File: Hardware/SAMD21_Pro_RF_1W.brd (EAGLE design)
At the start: 53.3 x 40.6 mm, 143 parts, among them J10 AVR_SPI_PROG_3X2TESTPOINTS, J12 JST, J13 U.FL, J14 RFM_DIO, J7 PTH, J9 External On/Off, U1 MCP73831, U2 ADJ3.3, U4 ATSAMD21G, U5 4MB Flash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

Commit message: Intermediate save
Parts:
- moved C12 39.5 mm to (22.9, 7.37), turned to 270 degrees
- moved C14 37.9 mm to (24.1, 7.37), turned to 90 degrees
- moved R8 28.3 mm to (29.2, 34.3), turned to 0 degrees
- moved J10 19.0 mm to (27.7, 25.4), turned to 180 degrees
- moved C8 15.1 mm to (23.6, 33.0), turned to 270 degrees
- moved C5 14.4 mm to (22.4, 33.0), turned to 90 degrees
- moved R3 10.7 mm to (24.9, 33.0), turned to 90 degrees
- moved C11 9.55 mm to (15.2, 36.8), turned to 270 degrees
- moved FD2 8.89 mm to (52.1, 36.8)
- moved FD4 8.89 mm to (52.1, 36.8)
- moved JP6 5.08 mm to (45.7, 14.0)
- moved JP1 5.08 mm to (45.7, 16.5)
- moved JP3 3.94 mm to (45.7, 31.1), turned to 180 degrees
- moved U5 2.59 mm to (29.2, 30.5)
- moved JP2 2.54 mm to (45.7, 19.1)
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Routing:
- net 5V: track 0.00 -> 86.8 mm, vias 0 -> 7
- net 3.3V: track 33.1 -> 103.1 mm, vias 4 -> 9
- net USB_VCC: track 0.96 -> 66.1 mm, vias 0 -> 5
- net GND: track 11.4 -> 73.6 mm, vias 5 -> 3
- net SCK: track 2.34 -> 64.6 mm, vias 1 -> 5
- net DIO3: track 0.00 -> 59.8 mm, vias 0 -> 5
- net DIO5: track 0.00 -> 57.0 mm, vias 0 -> 5
- net DIO4: track 0.00 -> 55.5 mm, vias 0 -> 5
- net DIO2: track 0.00 -> 54.1 mm, vias 0 -> 4
- net DIO1: track 0.00 -> 53.8 mm, vias 0 -> 3
- net !RST: track 12.6 -> 65.3 mm, vias 2 -> 3
- net DIO0: track 0.00 -> 52.6 mm, vias 0 -> 3
- net SDA: track 9.58 -> 60.1 mm, vias 1 -> 2
- net SCL: track 10.8 -> 59.0 mm, vias 1 -> 6
- net MISO: track 9.96 -> 57.6 mm, vias 1 -> 6
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- added copper zone on layer 1, net GND
- added copper zone on layer 16, net GND
- removed copper zone on layer 1, net GND1
- removed copper zone on layer 16, net GND1

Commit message: Intermediate
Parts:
- moved J7 0.64 mm to (1.91, 24.1)
- turned C6 to 90 degrees
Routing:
- net 3.3V: track 103.1 -> 212.6 mm, vias 9 -> 20
- net GND: track 73.6 -> 98.0 mm, vias 3 -> 36
- net RAW: track 41.3 -> 62.2 mm, vias 3 -> 6
- net 5V: track 86.8 -> 104.2 mm, vias 7 -> 8
- net MOSI: track 40.2 -> 57.6 mm, vias 4 -> 6
- net !RST: track 65.3 -> 72.6 mm, vias 3 -> 4
- net SHLD: track 0.00 -> 6.97 mm
- net USB_VCC: track 66.1 -> 71.8 mm
- net SWDCLK: track 25.4 -> 30.8 mm
- net MISO: track 57.6 -> 62.3 mm
- net D8_!FLASH_CS: track 20.4 -> 22.7 mm
- net SCK: track 64.6 -> 66.4 mm
- net D-: track 50.1 -> 51.8 mm
- net RXI: track 32.6 -> 34.3 mm
- net MISO5V: track 12.1 -> 13.5 mm
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- added copper zone on layer 1, net SHLD
- added copper zone on layer 16, net SHLD
- removed copper zone on layer 1, net SHLD1
- removed copper zone on layer 16, net SHLD1

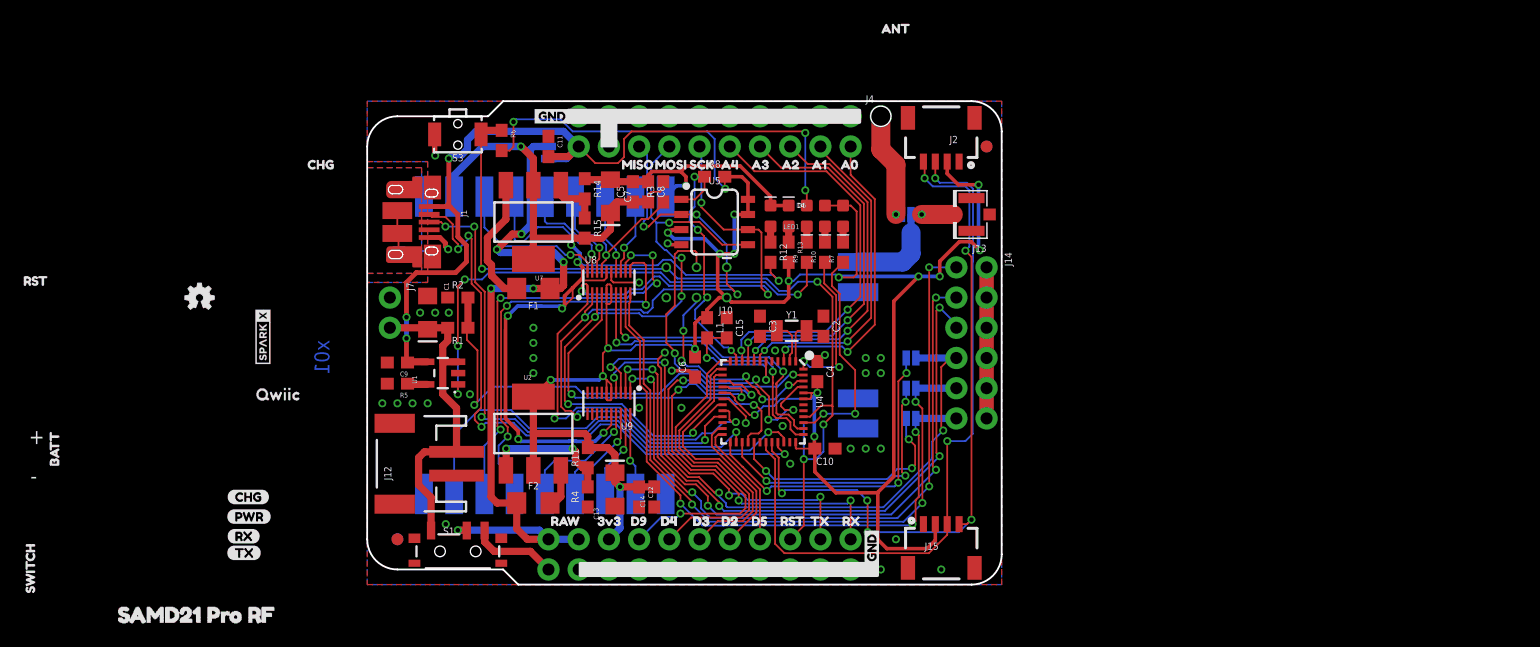
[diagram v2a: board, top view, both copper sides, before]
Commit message: Routed all wires
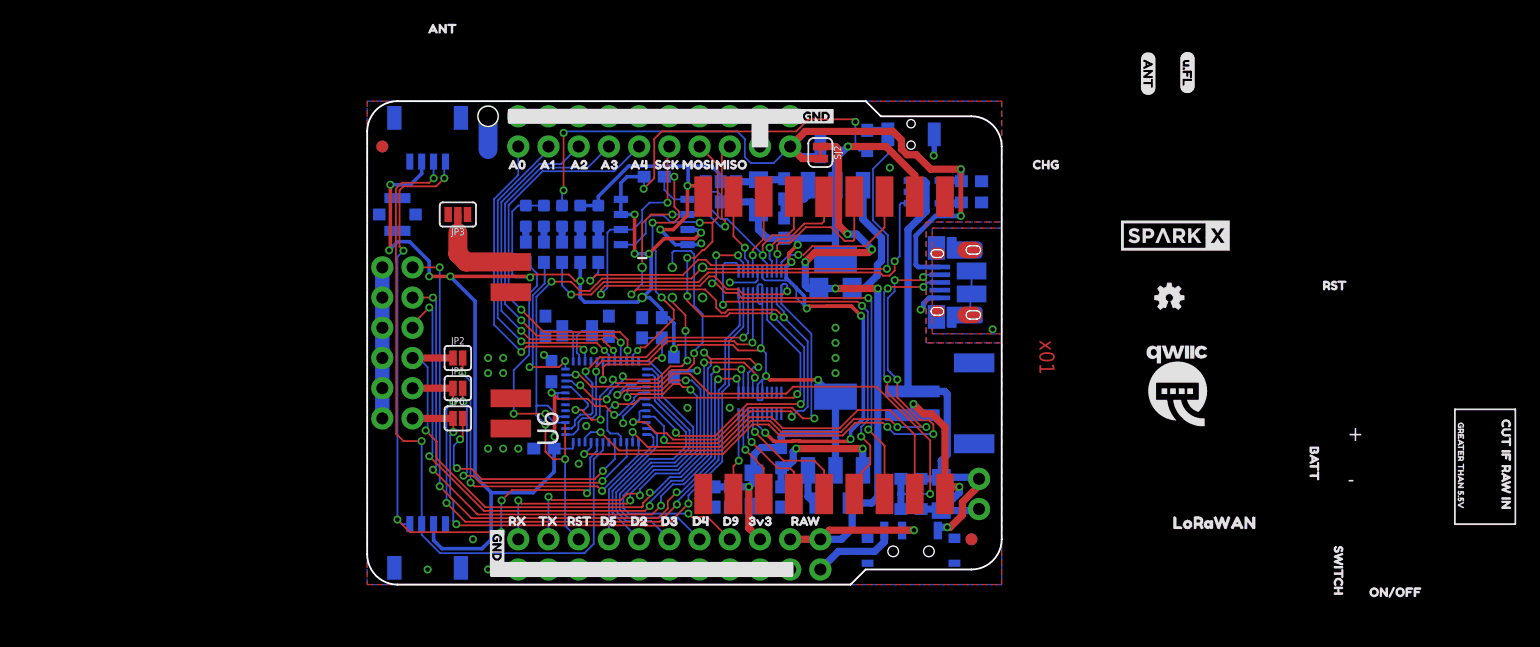
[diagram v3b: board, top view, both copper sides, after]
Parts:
- moved U$58 138.2 mm to (95.8, 14.6), flipped to the top
- moved U$59 130.6 mm to (91.9, 14.1), flipped to the top
- moved U$26 121.9 mm to (87.6, -14.0), flipped to the bottom
- moved U$39 113.8 mm to (83.6, -0.64), flipped to the top
- moved U$28 112.5 mm to (82.9, 25.5), flipped to the bottom
- moved U$27 110.0 mm to (81.7, -1.40), flipped to the bottom
- moved U$37 110.0 mm to (81.7, 3.94), flipped to the top
- moved U$29 105.9 mm to (79.6, 9.27), flipped to the bottom
- moved U$32 105.9 mm to (79.6, 12.3), flipped to the top
- moved U$36 105.9 mm to (79.6, 25.1), flipped to the top
- moved U$1 97.5 mm to (75.4, -2.54), flipped to the bottom
- moved U$35 87.1 mm to (70.2, 5.21), flipped to the top
- moved U$56 84.6 mm to (69.0, 44.8), flipped to the top
- moved U$30 82.8 mm to (68.1, 16.8), flipped to the top
- moved U$51 82.5 mm to (67.9, 29.3), flipped to the top
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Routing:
- net GND: track 98.0 -> 125.5 mm, vias 36 -> 31
- net VBATT: track 27.3 -> 41.1 mm, vias 0 -> 1
- net ANT_HEADER: track 9.24 -> 2.79 mm, vias 1 -> 0
- net USB_VCC: track 71.8 -> 66.2 mm, vias 5 -> 4
- net CHARGE_STAT: track 42.8 -> 38.0 mm, vias 4 -> 2
- net VBATT_LVL: track 39.7 -> 43.9 mm
- net N$3: track 2.67 -> 0.00 mm, vias 1 -> 0
- net SHLD: track 6.97 -> 4.54 mm, vias 0 -> 1
- net D8_!FLASH_CS: track 22.7 -> 24.3 mm
- net MOSI: track 57.6 -> 58.7 mm
- net D+: track 49.0 -> 50.1 mm, vias 4 -> 6
- net MISO: track 62.3 -> 63.4 mm
- net !RST: track 72.6 -> 73.7 mm
- net RAW: track 62.2 -> 62.7 mm
- net D-: track 51.8 -> 52.0 mm, vias 4 -> 6
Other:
- outline, holes or cut-outs redrawn

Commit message: Almost done
ToDo: Ask for guidance on antenna traces, double check on if the same chip is used (to know how to connect DIO pins), get board/schem review, order
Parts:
- removed U$1: (no value), SAMD21:SAMD21_PRO_RF0
- removed U$14, U$40: (no value), buzzard_labels (25):CHG1
- removed U$27, U$37: (no value), buzzard_labels (25):SWITCH23
- added U$64, U$75: (no value), buzzard_labels:IO00
- added U$66, U$76: (no value), buzzard_labels:IO11
- added U$67, U$77: (no value), buzzard_labels:IO22
- added U$68, U$78: (no value), buzzard_labels:IO33
- added U$71, U$79: (no value), buzzard_labels:IO44
- added U$74, U$80: (no value), buzzard_labels:IO55
- added U$81: (no value), buzzard_labels:SAMD21_PRORF_1W5
- moved U$26 121.9 mm to (-34.3, -14.0), flipped to the top
- moved U$58 84.1 mm to (14.6, 36.8), flipped to the bottom, turned to 0 degrees
- moved FRAME2 81.3 mm to (-14.0, -12.7), flipped to the top
- moved U$59 80.8 mm to (14.1, 35.8), flipped to the bottom, turned to 0 degrees
- moved U$28 77.6 mm to (5.97, 35.4), flipped to the top
- moved U$39 73.2 mm to (10.4, 1.91), flipped to the bottom
- moved U$36 71.7 mm to (9.27, 38.7), flipped to the bottom
- moved U$29 70.1 mm to (9.65, 5.46), flipped to the top
- moved U$32 69.3 mm to (10.3, 13.2), turned to 90 degrees
- moved LOGO1 66.1 mm to (2.54, 36.7), flipped to the bottom, turned to 270 degrees
- moved U$61 66.1 mm to (2.54, 36.7), flipped to the top, turned to 90 degrees
- moved FD2 50.8 mm to (52.1, 36.8), flipped to the bottom
- moved FD4 50.8 mm to (52.1, 36.8), flipped to the top
- moved U6 50.8 mm to (1.27, 7.62), flipped to the bottom
- moved J7 49.5 mm to (1.91, 6.35), flipped to the top
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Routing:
- net 3.3V: track 212.6 -> 204.0 mm
- net 5V: track 104.2 -> 100.3 mm
- net TX_LED: track 18.6 -> 16.5 mm
- net GND: track 125.5 -> 127.1 mm
- net SCK: track 66.7 -> 65.4 mm
- net USB_VCC: track 66.2 -> 67.5 mm
- net D9: track 28.4 -> 27.5 mm
- net D3: track 22.2 -> 21.3 mm
- net D4: track 24.9 -> 24.0 mm
- net RX_LED: track 13.2 -> 12.5 mm
- net TXO: track 34.8 -> 34.1 mm
- net RXI: track 34.3 -> 33.6 mm
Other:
- outline, holes or cut-outs redrawn

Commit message: Logging off
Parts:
- added U$1, U$14: (no value), buzzard_labels:VUSB7
- added U$27, U$37: (no value), buzzard_labels:SWITCH6
- moved U$24 1.27 mm to (16.0, 5.33)
- moved U$52 1.27 mm to (19.7, 5.33)
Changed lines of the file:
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@@
 <element name="U$13" library="buzzard_labels (25)" package="RST2" value="" x="34.036" y="5.334" smashed="yes"/>
 <element name="U$23" library="buzzard_labels (25)" package="3V320" value="" x="18.669" y="5.334" smashed="yes"/>
-<element name="U$24" library="buzzard_labels (25)" package="RAW21" value="" x="14.732" y="5.334" smashed="yes"/>
+<element name="U$24" library="buzzard_labels (25)" package="RAW21" value="" x="16.002" y="5.334" smashed="yes"/>
 <element name="U$28" library="buzzard_labels (25)" package="RST2" value="" x="5.969" y="35.433" smashed="yes"/>
 <element name="U$29" library="buzzard_labels (25)" package="BATT25" value="" x="9.652" y="5.461" smashed="yes" rot="R90"/>
@@
 <element name="U$49" library="buzzard_labels (25)" package="SCK10" value="" x="29.845" y="35.306" rot="MR0"/>
 <element name="U$50" library="buzzard_labels (25)" package="ANT11" value="" x="45.085" y="37.846" rot="MR0"/>
-<element name="U$52" library="buzzard_labels (25)" package="RAW21" value="" x="18.415" y="5.334" rot="MR0"/>
+<element name="U$52" library="buzzard_labels (25)" package="RAW21" value="" x="19.685" y="5.334" rot="MR0"/>
 <element name="U$53" library="buzzard_labels (25)" package="3V320" value="" x="21.971" y="5.334" rot="MR0"/>
 <element name="J12" library="SparkFun-Connectors" package="JST-2-SMD" value="JST" x="3.81" y="15.24" rot="R90">
@@
 <element name="U$80" library="buzzard_labels" package="IO55" value="" x="47.625" y="25.146" rot="R90"/>
 <element name="U$81" library="buzzard_labels" package="SAMD21_PRORF_1W5" value="" x="23.495" y="11.684" rot="R90"/>
+<element name="U$1" library="buzzard_labels" package="VUSB7" value="" x="15.621" y="35.306"/>
+<element name="U$14" library="buzzard_labels" package="VUSB7" value="" x="20.066" y="35.306" rot="MR0"/>
+<element name="U$27" library="buzzard_labels" package="SWITCH6" value="" x="13.462" y="0.254" rot="R90"/>
+<element name="U$37" library="buzzard_labels" package="SWITCH6" value="" x="13.462" y="4.953" rot="MR270"/>
 </elements>
 <signals>

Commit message: Updates from board review
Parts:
- removed F2: 6V/0.75A, SparkFun-Fuses:1206
- removed J14: RFM_DIO, SparkFun-Connectors:2X6_NOSILK
- removed JP1, JP2: (no value), SparkFun-Jumpers:SMT-JUMPER_2_NO_SILK
- removed JP3: JUMPER-SMT_3_1-NC_PASTE_SILK, SparkFun-Jumpers:SMT-JUMPER_3_1-NC_PASTE_SILK
- removed JP6: JUMPER-SMT_2_NC_PASTE_SILK, SparkFun-Jumpers:SMT-JUMPER_2_NC_PASTE_SILK
- removed LED2: RED, SparkFun-LED:LED-0603
- removed R12: 1k, SparkFun-Resistors:0603
- removed U$54: (no value), ANT:ANT0
- removed U$56: (no value), ufl:U#FL0
- removed U$64, U$75: (no value), buzzard_labels:IO00
- removed U$66, U$76: (no value), buzzard_labels:IO11
- removed U$67, U$77: (no value), buzzard_labels:IO22
- removed U$68, U$78: (no value), buzzard_labels:IO33
- removed U$71, U$79: (no value), buzzard_labels:IO44
- removed U$74, U$80: (no value), buzzard_labels:IO55
- D4: value Yellow -> BLUE
- moved U$60 28.4 mm to (50.4, 17.7)
- moved U$51 22.6 mm to (48.3, 20.3)
- moved U$81 21.8 mm to (45.3, 11.4)
- moved FD1 5.18 mm to (7.62, 2.79)
- moved FD3 5.18 mm to (7.62, 2.79)
- moved J7 2.62 mm to (1.27, 3.81)
- moved J4 2.54 mm to (43.2, 36.8)
- moved U$11 2.54 mm to (41.3, 35.3)
- moved U$50 2.54 mm to (45.1, 35.3)
- moved R8 1.27 mm to (30.5, 34.3)
- moved U5 1.27 mm to (30.6, 30.5)
- moved R1 0.89 mm to (8.51, 8.89)
- moved R2 0.89 mm to (8.51, 6.35)
- moved U$63 0.76 mm to (35.4, 31.1)
- moved R3 0.58 mm to (25.7, 33.0)
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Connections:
- removed net ANT_HEADER: J4.1, JP3.1
- removed net DIO0: J14.11, JP6.1, U8.9
- removed net DIO1: J14.9, JP1.1, U8.10
- removed net DIO2: J14.7, JP2.1, U9.4
- removed net DIO3: J14.5, U9.3
- removed net DIO35V: U6.P$4, U9.18
- removed net DIO4: J14.3, U9.2
- removed net DIO45V: U6.P$3, U9.19
- removed net DIO5: J14.1, U9.1
- removed net DIO55V: U6.P$2, U9.20
- removed net N$10: LED2.A, R12.1
- removed net N$3: J13.FEED, JP3.3
- removed net N$4: F2.2, U2.3
- net 5V: no longer R12.2
- net ANT: now also J13.FEED, J4.1; no longer JP3.2
- net D10: now also U8.10; no longer JP1.2
- net D11: now also U9.4; no longer JP2.2
- net GND: no longer J14.10, J14.12, J14.2, J14.4, J14.6, J14.8, LED2.C
- net N$12: now also F1.1, SJ2.2; no longer F1.2, U7.3
- net RAW: now also U2.3, U7.3; no longer F1.1, F2.1
- net RFM_INT: now also U8.9; no longer JP6.2
- net USB_VCC: now also F1.2; no longer SJ2.2
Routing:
- net DIO3: track 59.1 -> 0.00 mm, vias 5 -> 0
- net DIO5: track 56.8 -> 0.00 mm, vias 5 -> 0
- net DIO4: track 55.4 -> 0.00 mm, vias 5 -> 0
- net DIO1: track 53.9 -> 0.00 mm, vias 3 -> 0
- net DIO2: track 53.2 -> 0.00 mm, vias 4 -> 0
- net DIO0: track 52.6 -> 0.00 mm, vias 3 -> 0
- net 3.3V: track 204.0 -> 240.3 mm, vias 20 -> 21
- net 5V: track 100.3 -> 70.2 mm, vias 8 -> 5
- net GND: track 127.1 -> 114.3 mm, vias 31 -> 28
- net RFM_INT: track 20.4 -> 30.8 mm, vias 3 -> 2
- net N$12: track 11.0 -> 21.3 mm, vias 0 -> 1
- net ANT: track 8.04 -> 17.5 mm, vias 0 -> 1
- net DIO35V: track 8.92 -> 0.00 mm, vias 1 -> 0
- net D10: track 23.7 -> 31.2 mm, vias 3 -> 2
- net DIO45V: track 7.43 -> 0.00 mm, vias 1 -> 0
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- added copper zone on layer 1, net ANT
- added copper zone on layer 16, net ANT

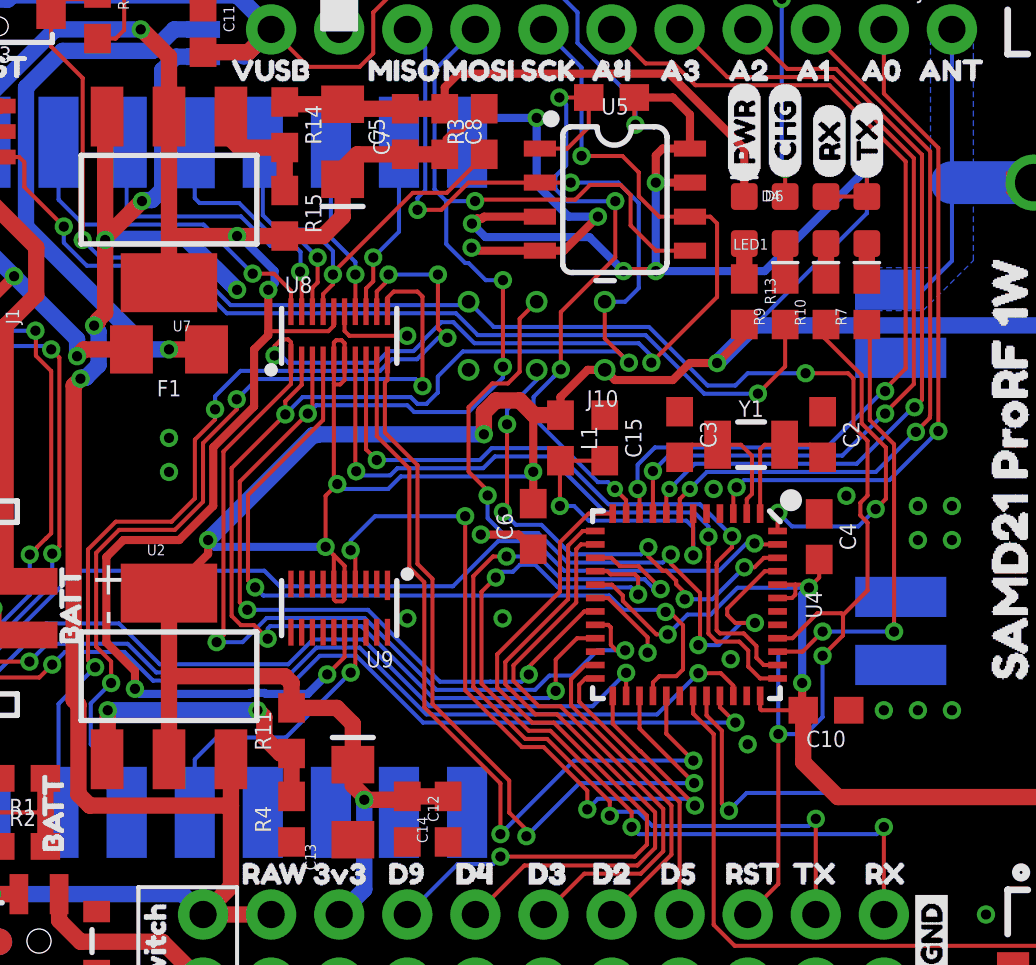
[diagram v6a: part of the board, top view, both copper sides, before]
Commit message: Increased power trace width
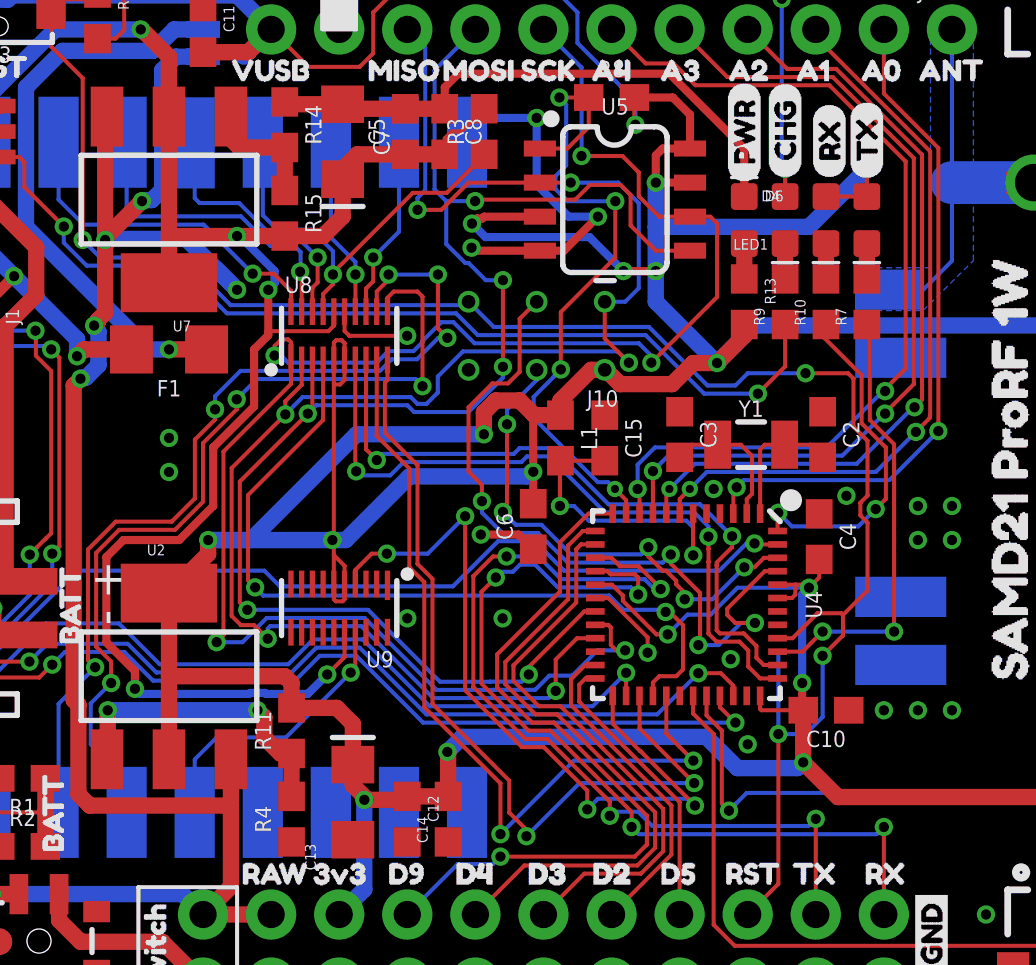
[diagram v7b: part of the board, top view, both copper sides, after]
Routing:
- net 3.3V: track 240.3 -> 252.9 mm, vias 21 -> 22
- net D11: track 29.3 -> 28.4 mm

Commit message: Updated power supply in schematic
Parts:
- removed R11: 470, SparkFun-Resistors:0603
- removed R4: 787, SparkFun-Resistors:0603
- removed SJ2: USB Power, SparkFun-Jumpers:SMT-JUMPER_2_NC_TRACE_SILK
- removed U2: ADJ3.3, SparkFun-IC-Power:SOT223
- removed U9: TXB0108DQSR, SparkFun-IC-Comms:UFDFN-20
- added D2: 3A/40V/500mV, SparkFun-DiscreteSemi:SMA-DIODE
- added D3, D5: 3A/10V/300mV, SAMD21_ProRF_1W:SOD-323
- added JP1: FuseBypass, SparkFun-Jumpers:SMT-JUMPER_2_NO_SILK
- added Q1: 310mA/60V/1.6Ω, SparkFun-DiscreteSemi:SOT323
- added R12, R16: 10k, SparkFun-Resistors:0603
- added U3: 3.3V, SparkFun-IC-Power:SOT23-5
- F1: value 6V/0.75A -> 6V 0.5A; device SparkFun-Fuses:1206 -> SparkFun-Fuses:0805
- J12: value JST -> 5.5x2.1mm Barrel; device SparkFun-Connectors:JST-2-SMD -> SparkFun-Connectors:POWER_JACK_SMD
- R14: value 715 -> 750K
- moved J12 96.8 mm to (-38.4, -71.9), turned to 0 degrees
- moved U$32 0.13 mm to (10.4, 13.2)
- moved U$72 0.13 mm to (38.5, 31.2)
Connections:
- removed net N$5: R11.1, R4.2, U2.1
- new net N$14: D5.A, R15.2, U7.2, U7.4
- new net N$4: D2.A, J12.VIN0
- net !RFM_CS: now also Q1.2, R12.1; no longer U8.4
- net !RFM_CS5V: now also Q1.3, R16.1; no longer U8.17
- net 3.3V: now also Q1.1, R12.2, U3.5; no longer R11.2, U2.2, U2.4, U9.5, U9.6
- net 5V: now also D3.C, D5.C, R16.2, U3.1, U3.3; no longer R15.2, U7.2, U7.4, U9.16
- net D11: now also U8.4; no longer U9.4
- net DIO25V: now also U8.17; no longer U9.17
- net GND: now also J12.P$4, U3.2; no longer J12.1, R4.1, U9.15
- net N$12: now also D3.A, JP1.1; no longer SJ2.2
- net RAW: no longer SJ2.1, U2.3
- net USB_VCC: now also JP1.2
- net VBATT: now also D2.C; no longer J12.2
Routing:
- net N$12: track 21.3 -> 0.00 mm, vias 1 -> 0
- net 3.3V: track 252.9 -> 234.0 mm
- net 5V: track 70.2 -> 56.8 mm
- net N$5: track 11.4 -> 0.00 mm, vias 2 -> 0
- net VBATT: track 44.1 -> 40.9 mm
- net RAW: track 65.8 -> 63.0 mm
- net !RFM_CS: track 29.8 -> 27.5 mm
- net DIO25V: track 10.7 -> 9.38 mm
- net !RFM_CS5V: track 15.9 -> 15.2 mm
- net D11: track 28.4 -> 27.9 mm
- net USB_VCC: track 73.2 -> 73.7 mm
- net ANT: track 17.5 -> 17.9 mm, vias 1 -> 3
